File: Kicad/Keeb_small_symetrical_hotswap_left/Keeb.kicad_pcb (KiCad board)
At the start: 2 copper layers, 96.2 x 98.1 mm, 32 parts, among them J1 TYPE-C-31-M-12, J2 B2B-XH-A_LF__SN_, SW1 CherryMX, SW10 CherryMX, SW11 CherryMX, SW13 CherryMX, SW14 CherryMX, SW15 CherryMX, SW16 CherryMX, SW17 CherryMX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

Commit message: Initial commit
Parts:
- removed SW2: CherryMX, ScottoKeebs_Hotswap:Hotswap_MX_Plated_1.00u_Smaller_hole
- removed U1: Pico, MCU_RaspberryPi_and_Boards:RPi_Pico_SMD_TH_NO_BACK_HOLES
- added U3: nice_nano, Nice_nano:nice_nano, B.Cu at (172.9, 112.0)
- J1: value TYPE-C-31-M-12 -> MJ-4PP-9_MJ-4PP-9; footprint TypeC:HRO_TYPE-C-31-M-12 -> MJ-4PP-9:MJ-4PP-9
- SW1, SW10, SW11, SW13, SW14, SW15, SW16, SW17, SW18, SW19, SW20, SW3, SW4, SW5, SW6, SW7, SW8, SW9: footprint ScottoKeebs_Hotswap:Hotswap_MX_Plated_1.00u_Smaller_hole -> ScottoKeebs_Hotswap:Hotswap_MX_Plated_1.00u
- moved J1 4.11 mm to (131.6, 39.8), turned to -90 degrees
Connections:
- J2 pad 1: VSYS -> 3v3
- SW1 pad 1: 27 -> 2
- SW10 pad 1: 12 -> 13
- SW11 pad 1: 13 -> 12
- SW13 pad 1: GND -> 9
- SW13 pad 2: 19 -> GND
- SW14 pad 1: GND -> 7
- SW14 pad 2: 18 -> GND
- SW15 pad 2: 21 -> 5
- SW16 pad 1: 20 -> 1
- SW17 pad 1: 16 -> 8
- SW18 pad 1: 17 -> 6
- SW19 pad 1: 22 -> 4
- SW20 pad 1: 26 -> 3
- SW3 pad 2: 7 -> 19
- SW4 pad 2: 6 -> 20
- SW5 pad 2: 5 -> 21
- SW6 pad 2: 9 -> 15
- SW7 pad 2: 8 -> 16
- SW8 pad 2: 10 -> 17
- SW9 pad 1: 11 -> 14
- U2 pad CLK: 4 -> 11
- U2 pad DT: 3 -> 10
- U2 pad SW: 28 -> unconnected-(U2-PadSW)
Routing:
- net VSYS: track 119.0 -> 0.00 mm
- net 3v3: track 286.9 -> 168.7 mm
- net 28: track 116.2 -> 0.00 mm
- net GND: track 605.9 -> 499.0 mm
- net 3: track 155.1 -> 61.8 mm
- net 4: track 152.7 -> 63.1 mm
- net 10: track 15.5 -> 100.7 mm
- net 2: track 107.5 -> 22.8 mm
- net 18: track 47.0 -> 113.0 mm
- net 22: track 61.0 -> 0.00 mm
- net 26: track 48.0 -> 0.00 mm
- net 8: track 49.1 -> 88.0 mm
- net 13: track 16.4 -> 53.0 mm
- net 5: track 21.1 -> 56.7 mm
- net 21: track 56.5 -> 21.4 mm
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
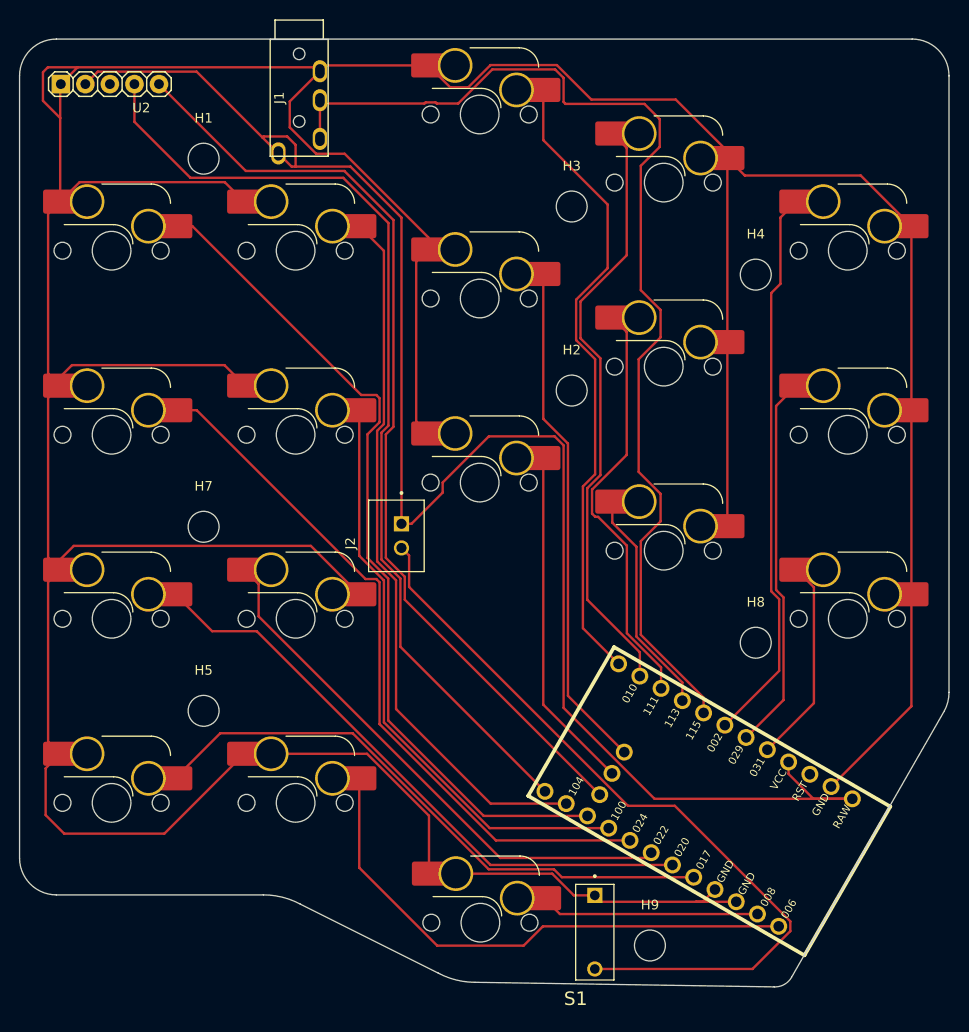
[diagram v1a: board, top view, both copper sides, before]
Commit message: current version, all problems fixed, software compiled for CP 9.0
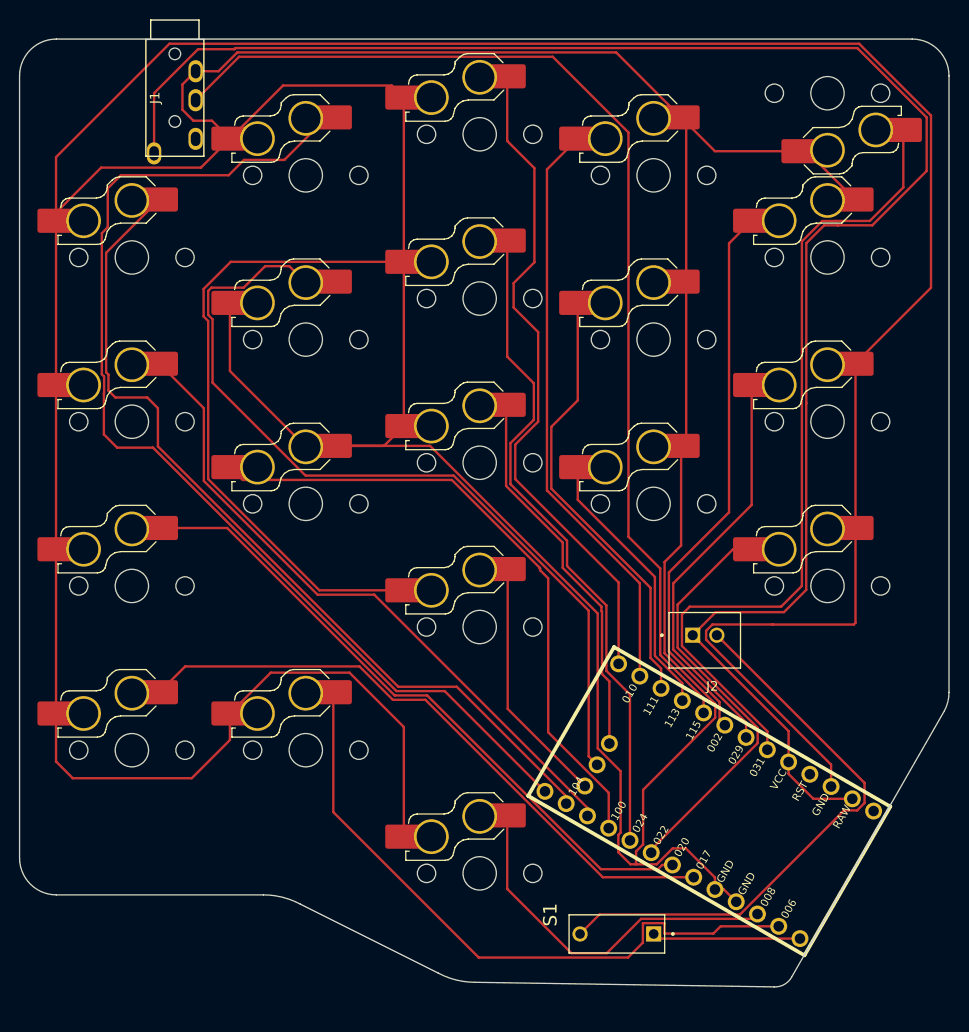
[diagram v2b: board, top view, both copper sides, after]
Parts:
- removed H1, H2, H3, H4, H5, H7, H8, H9: MountingHole, MountingHole:MountingHole_3.2mm_M3
- removed U2: KY-040, KY-040:KY-040-PORT
- added SW12: CherryMX, ScottoKeebs_Hotswap:Hotswap_Choc_V1_Plated_1.00u, B.Cu at (186.2, 39.3)
- added SW2: CherryMX, ScottoKeebs_Hotswap:Hotswap_Choc_V1_Plated_1.00u, B.Cu at (150.2, 94.6)
- SW1, SW10, SW11, SW13, SW14, SW15, SW16, SW17, SW18, SW19, SW20, SW3, SW4, SW5, SW6, SW7, SW8, SW9: footprint ScottoKeebs_Hotswap:Hotswap_MX_Plated_1.00u -> ScottoKeebs_Hotswap:Hotswap_Choc_V1_Plated_1.00u
- moved J2 33.7 mm to (173.5, 95.9), turned to 180 degrees
- moved J1 12.9 mm to (118.7, 39.8)
- moved SW15 11.9 mm to (132.2, 81.8)
- moved SW14 9.91 mm to (132.2, 64.8)
- moved SW13 7.87 mm to (132.2, 47.8)
- moved SW20 5.84 mm to (114.2, 107.3)
- moved SW16 5.55 mm to (132.2, 107.3)
- moved SW1 5.11 mm to (150.2, 120.1)
- moved SW8 4.96 mm to (168.2, 81.8)
- moved SW19 4.00 mm to (114.2, 90.3)
- moved SW5 4.00 mm to (186.2, 90.3)
- moved SW7 2.99 mm to (168.2, 64.8)
- moved SW18 2.50 mm to (114.2, 73.3)
- moved SW4 2.50 mm to (186.2, 73.3)
- moved S1 2.29 mm to (164.4, 126.3), turned to 90 degrees
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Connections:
- J1 pad 4: 18 -> unconnected-(J1-D-Pad4)
- S1 pad 1A: GND -> B-
- SW10 pad 1: 13 -> 6
- SW11 pad 1: 12 -> 13
- SW13 pad 1: 9 -> 10
- SW14 pad 1: 7 -> 12
- SW15 pad 2: 5 -> 7
- SW17 pad 1: 8 -> 9
- SW18 pad 1: 6 -> 8
- SW5 pad 2: 21 -> 5
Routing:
- net GND: track 499.0 -> 727.9 mm
- net 11: track 99.1 -> 25.8 mm
- net 21: track 21.4 -> 85.7 mm
- net 12: track 35.6 -> 86.6 mm
- net Net-(J2-Pad2): track 81.0 -> 58.8 mm
- net 8: track 88.0 -> 68.6 mm
- net 3v3: track 168.7 -> 187.9 mm
- net 9: track 73.8 -> 90.0 mm
- net B-: track 0.00 -> 15.3 mm
- net 2: track 22.8 -> 37.9 mm
- net 13: track 53.0 -> 39.5 mm
- net 5: track 56.7 -> 43.7 mm
- net 10: track 100.7 -> 113.2 mm
- net 1: track 56.8 -> 68.8 mm
- net 7: track 61.2 -> 69.1 mm
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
